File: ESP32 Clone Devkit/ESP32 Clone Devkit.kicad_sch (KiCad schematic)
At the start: 34 parts, among them J1 USB_B_Micro, J2 Conn_01x19_Pin, J3 Conn_01x19_Pin, Q1 MMSS8050-H-TP, Q2 MMSS8050-H-TP, SW1 SW_Push, SW2 SW_Push, U1 CP2102N-A02-GQFN28, U2 AMS1117-3.3

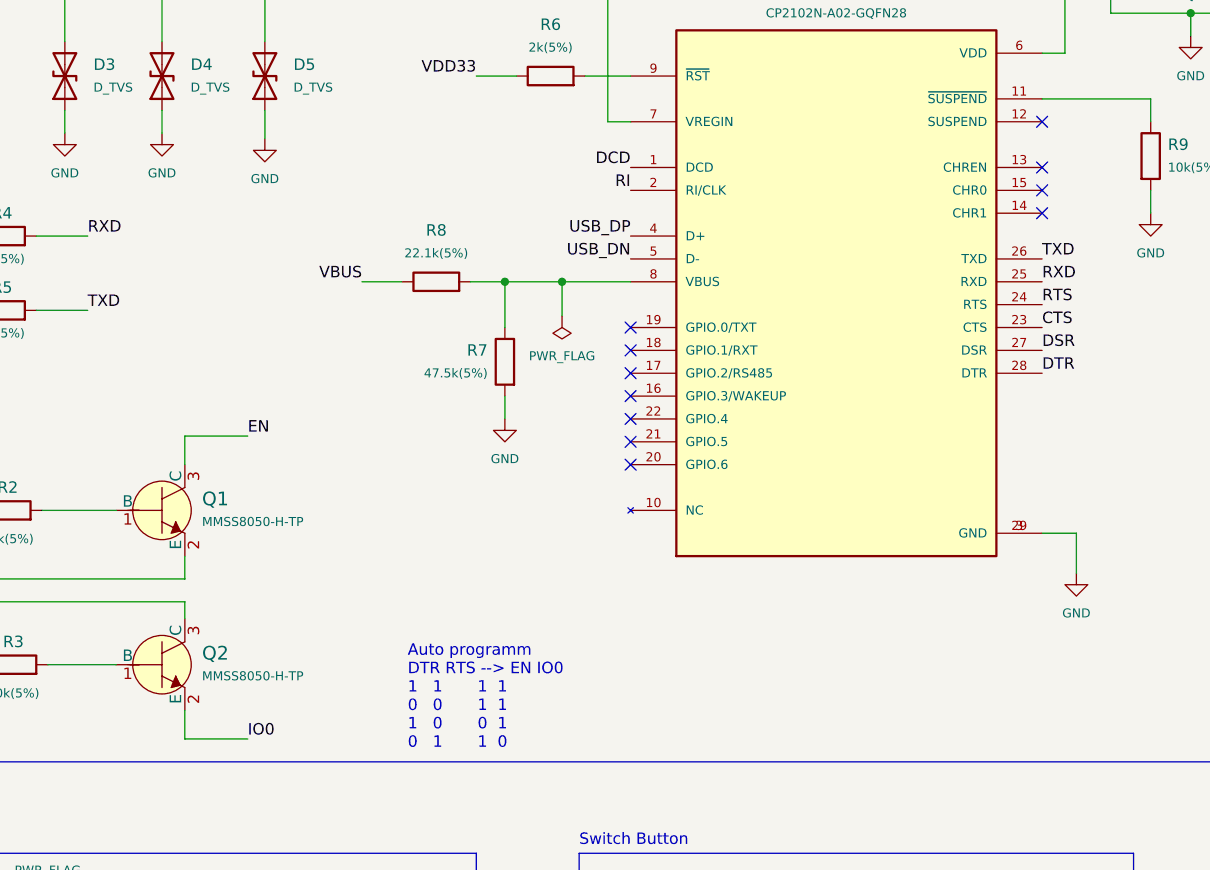
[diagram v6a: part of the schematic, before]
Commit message: mark unused pins
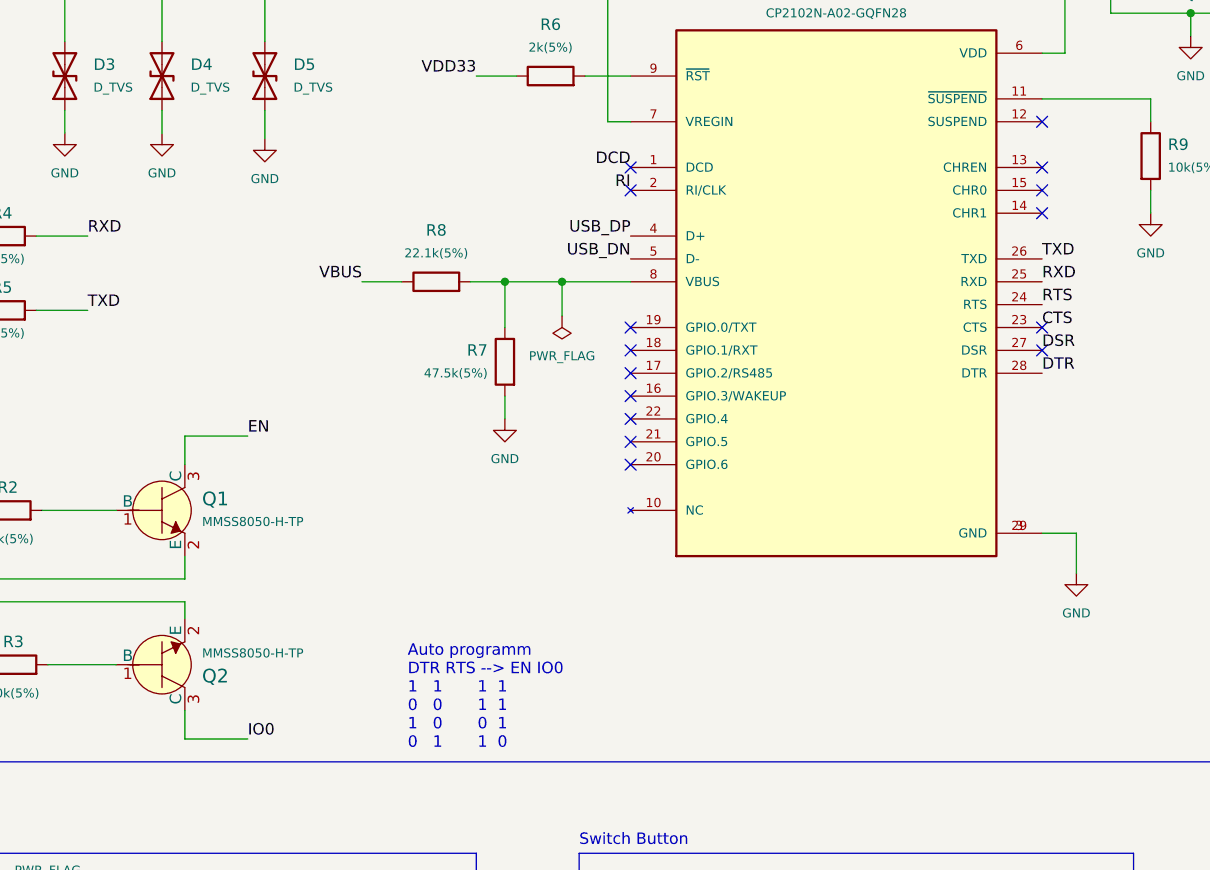
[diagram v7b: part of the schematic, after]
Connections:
- net DTR: now also Q2.2 (E); no longer Q2.3 (C)
- net IO0: now also Q2.3 (C); no longer Q2.2 (E)
- no-connect marks 12 -> 16
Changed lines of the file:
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@@
   )
   (no_connect (at 104.14 99.06))
+  (no_connect (at 104.14 68.58))
   (no_connect (at 149.86 68.58))
   (no_connect (at 104.14 86.36))
@@
   (no_connect (at 34.29 45.085))
   (no_connect (at 104.14 93.98))
+  (no_connect (at 149.86 83.82))
+  (no_connect (at 104.14 66.04))
   (no_connect (at 104.14 88.9))
+  (no_connect (at 149.86 86.36))
   (wire (pts (xy 101.6 60.96) (xy 101.6 44.45))
     (stroke (width 0) (type default))
@@
     )
   )
-  (symbol (lib_id "dk_Transistors-Bipolar-BJT-Single:MMSS8050-H-TP") (at 52.07 121.285 0) (unit 1)
-    (in_bom yes) (on_board yes) (dnp no) (fields_autoplaced)
-    (property "Reference" "Q2" (at 56.515 120.015 0)
+  (symbol (lib_id "dk_Transistors-Bipolar-BJT-Single:MMSS8050-H-TP") (at 52.07 121.285 0) (mirror x) (unit 1)
+    (in_bom yes) (on_board yes) (dnp no)
+    (property "Reference" "Q2" (at 56.515 122.555 0)
       (effects (font (size 1.524 1.524)) (justify left))
     )
-    (property "Value" "MMSS8050-H-TP" (at 56.515 122.555 0)
+    (property "Value" "MMSS8050-H-TP" (at 56.515 120.015 0)
       (effects (font (size 1 1)) (justify left))
     )
-    (property "Footprint" "digikey-footprints:SOT-23-3" (at 57.15 116.205 0)
-      (effects (font (size 1.524 1.524)) (justify left) hide)
-    )
-    (property "Datasheet" "https://www.mccsemi.com/pdf/Products/MMSS8050(SOT-23).pdf" (at 57.15 113.665 0)
-      (effects (font (size 1.524 1.524)) (justify left) hide)
-    )
-    (property "Digi-Key_PN" "MMSS8050-H-TPMSCT-ND" (at 57.15 111.125 0)
-      (effects (font (size 1.524 1.524)) (justify left) hide)
-    )
-    (property "MPN" "MMSS8050-H-TP" (at 57.15 108.585 0)
-      (effects (font (size 1.524 1.524)) (justify left) hide)
-    )
-    (property "Category" "Discrete Semiconductor Products" (at 57.15 106.045 0)
-      (effects (font (size 1.524 1.524)) (justify left) hide)
-    )
-    (property "Family" "Transistors - Bipolar (BJT) - Single" (at 57.15 103.505 0)
-      (effects (font (size 1.524 1.524)) (justify left) hide)
-    )
-    (property "DK_Datasheet_Link" "https://www.mccsemi.com/pdf/Products/MMSS8050(SOT-23).pdf" (at 57.15 100.965 0)
-      (effects (font (size 1.524 1.524)) (justify left) hide)
-    )
-    (property "DK_Detail_Page" "/product-detail/en/micro-commercial-co/MMSS8050-H-TP/MMSS8050-H-TPMSCT-ND/2825945" (at 57.15 98.425 0)
-      (effects (font (size 1.524 1.524)) (justify left) hide)
-    )
-    (property "Description" "TRANS NPN 25V 1.5A SOT23" (at 57.15 95.885 0)
-      (effects (font (size 1.524 1.524)) (justify left) hide)
-    )
-    (property "Manufacturer" "Micro Commercial Co" (at 57.15 93.345 0)
-      (effects (font (size 1.524 1.524)) (justify left) hide)
-    )
-    (property "Status" "Active" (at 57.15 90.805 0)
+    (property "Footprint" "digikey-footprints:SOT-23-3" (at 57.15 126.365 0)
+      (effects (font (size 1.524 1.524)) (justify left) hide)
+    )
+    (property "Datasheet" "https://www.mccsemi.com/pdf/Products/MMSS8050(SOT-23).pdf" (at 57.15 128.905 0)
+      (effects (font (size 1.524 1.524)) (justify left) hide)
+    )
+    (property "Digi-Key_PN" "MMSS8050-H-TPMSCT-ND" (at 57.15 131.445 0)
+      (effects (font (size 1.524 1.524)) (justify left) hide)
+    )
+    (property "MPN" "MMSS8050-H-TP" (at 57.15 133.985 0)
+      (effects (font (size 1.524 1.524)) (justify left) hide)
+    )
+    (property "Category" "Discrete Semiconductor Products" (at 57.15 136.525 0)
+      (effects (font (size 1.524 1.524)) (justify left) hide)
+    )
+    (property "Family" "Transistors - Bipolar (BJT) - Single" (at 57.15 139.065 0)
+      (effects (font (size 1.524 1.524)) (justify left) hide)
+    )
+    (property "DK_Datasheet_Link" "https://www.mccsemi.com/pdf/Products/MMSS8050(SOT-23).pdf" (at 57.15 141.605 0)
+      (effects (font (size 1.524 1.524)) (justify left) hide)
+    )
+    (property "DK_Detail_Page" "/product-detail/en/micro-commercial-co/MMSS8050-H-TP/MMSS8050-H-TPMSCT-ND/2825945" (at 57.15 144.145 0)
+      (effects (font (size 1.524 1.524)) (justify left) hide)
+    )
+    (property "Description" "TRANS NPN 25V 1.5A SOT23" (at 57.15 146.685 0)
+      (effects (font (size 1.524 1.524)) (justify left) hide)
+    )
+    (property "Manufacturer" "Micro Commercial Co" (at 57.15 149.225 0)
+      (effects (font (size 1.524 1.524)) (justify left) hide)
+    )
+    (property "Status" "Active" (at 57.15 151.765 0)
       (effects (font (size 1.524 1.524)) (justify left) hide)
     )
@@
       (effects (font (size 1.27 1.27)) hide)
     )
-    (pin "1")
+    (property "Purpose" "" (at 41.275 55.88 0)
+      (effects (font (size 1.27 1.27)))
+    )
+    (pin "1")
